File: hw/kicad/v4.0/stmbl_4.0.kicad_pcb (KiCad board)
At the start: 2 copper layers, 100 x 100 mm, 433 parts, among them J1 RJ45_LED, J2 RJ45_LED, J3 RJ45_LED, P1 USB_OTG, P10 CONN_02X06, P11 USB_OTG, P12 CONN_01X04, P13 CONN_01X04, P14 CONN_01X04, P15 CONN_01X02, P2 CONN_01X02, P3 CONN_01X02, P4 CONN_01X02, P5 CONN_01X06, P6 CONN_01X02, P7 CONN_01X04, P8 CONN_01X03, P9 CONN_01X06, Q1 IRLML6344, Q2 IRLML6344, Q3 IRLML6344, Q4 IRLML6344, Q5 IRLML6344, T1 testpoint, T2 testpoint, T44 testpoint, T45 testpoint, T46 testpoint, U1 USBLC6-4SC6, U10 SN65176B, U11 SN65176B, U12 IRAM256a, U13 ACT4088, U14 SN65176B, U15 SN65176B, U16 SN65176B, U17 SN65176B, U18 SN65176B, U19 SN65176B, U2 zldo1117, U20 USBLC6-4SC6, U21 USBLC6-4SC6, U22 USBLC6-4SC6, U23 USBLC6-4SC6, U24 non_plated, U25 STM32F303CBTx, U26 STM32F405VG, U27 ACT4088, U28 ACT4088, U29 USBLC6-4SC6, U3 SI8621, U30 non_plated, U31 non_plated, U32 non_plated, U33 heatsink, U34 fan, U35 non_plated, U36 non_plated, U37 non_plated, U39 non_plated, U4 ACT4088, U5 LNK304D, U6 LM358, U7 LM358, U8 SN65176B, U9 SN65176B, Y1 8M, Y2 8M

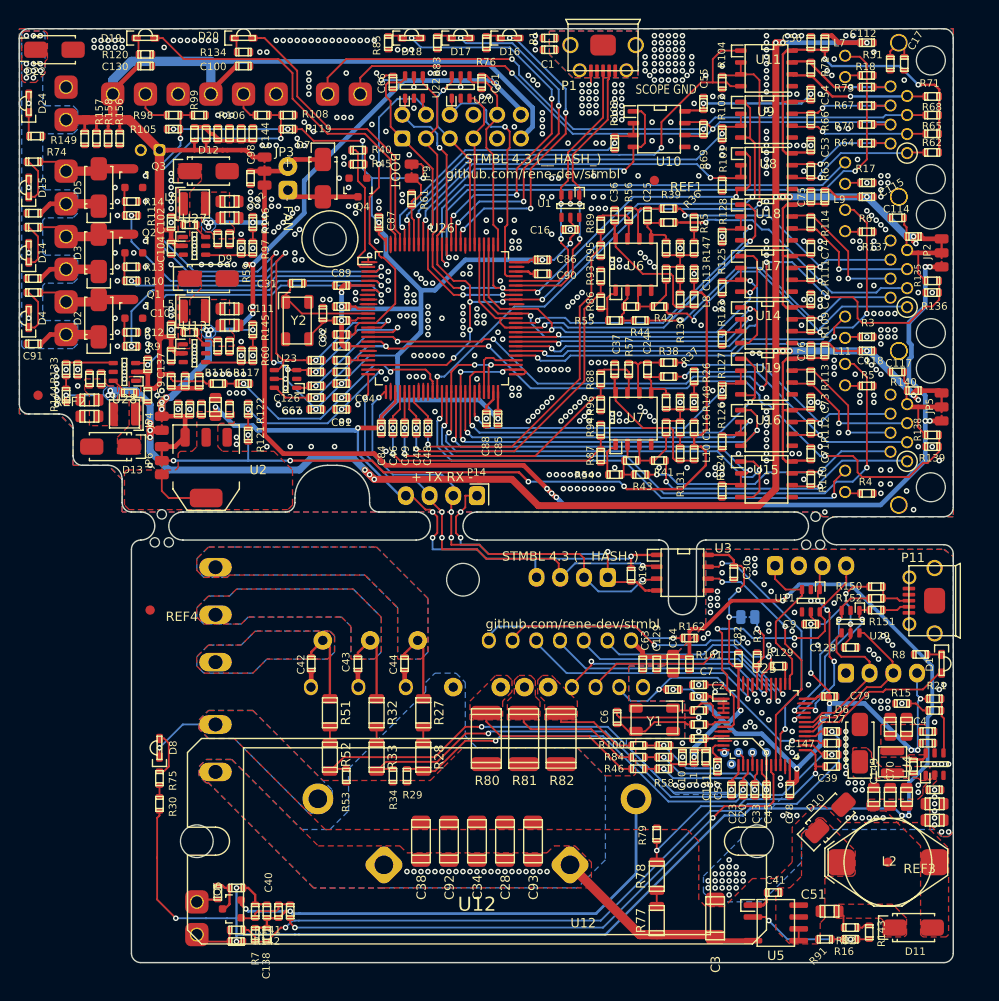
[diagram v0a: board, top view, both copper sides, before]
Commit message: Version for ST IGBT Modules
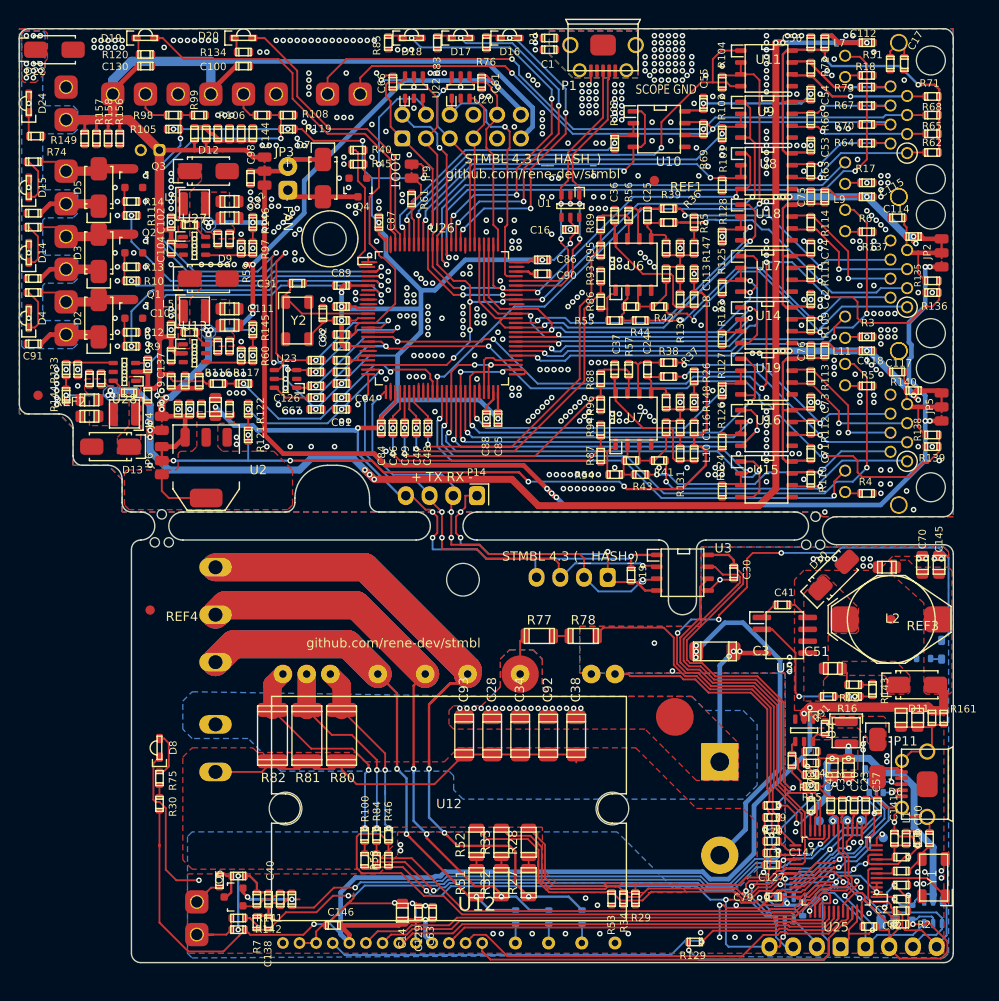
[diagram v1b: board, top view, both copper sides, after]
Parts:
- removed C22: 270µ, stmbl:C_Radial_D26_L45_P10
- removed R162: 1k, stmbl:R_0603
- added C146: 100n, stmbl:C_0603, F.Cu at (131.6, 145.8)
- C128, C9, D1, R150, R151, R152, R8, U21, U29: moved to B.Cu
- C21: value 270µ -> 560µ; footprint stmbl:C_Radial_D26_L45_P10 -> Capacitor_THT:CP_Radial_D30.0mm_P10.00mm_SnapIn
- C42, C43, C44: value 2.2µ -> 3.3µ; moved to B.Cu
- U12: value IRAM256a -> STGIBxx; footprint stmbl:IRAM256 -> stmbl:SDIP2B-26L
- moved U31 42.1 mm to (145.5, 108.8)
- moved P12 41.9 mm to (188.6, 148.0)
- moved C14 39.4 mm to (139.0, 144.4), turned to 270 degrees
- moved C129 36.9 mm to (140.8, 144.4), turned to 90 degrees
- moved JP1 35.9 mm to (191.0, 145.4)
- moved C6 35.9 mm to (195.5, 136.5)
- moved U21 35.8 mm to (195.8, 144.4), turned to 90 degrees
- moved C63 34.9 mm to (142.3, 144.4), turned to 90 degrees
- moved C42 34.9 mm to (151.1, 144.9), turned to 90 degrees
- moved Y1 34.3 mm to (195.9, 140.7), turned to 180 degrees
- moved R107 34.3 mm to (135.0, 138.8), turned to 270 degrees
- moved C43 34.0 mm to (154.7, 144.9), turned to 90 degrees
- moved C44 33.1 mm to (158.2, 144.9), turned to 90 degrees
- moved R77 33.0 mm to (153.7, 114.8), turned to 0 degrees
- moved C9 32.7 mm to (193.6, 144.4), turned to 270 degrees
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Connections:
- net /hv/f3/USB_DM renamed /hv/f3/USB_N
- net /hv/f3/USB_DP renamed /hv/f3/USB_P
- C42 pad 1: /hv/back-emf/W -> Net-(C42-Pad1)
- C42 pad 2: Net-(C42-Pad2) -> /hv/back-emf/W
- C43 pad 1: /hv/back-emf/V -> Net-(C43-Pad1)
- C43 pad 2: Net-(C43-Pad2) -> /hv/back-emf/V
- C44 pad 1: /hv/back-emf/U -> Net-(C44-Pad1)
- C44 pad 2: Net-(C44-Pad2) -> /hv/back-emf/U
- P1 pad 1: (no net) -> Net-(P1-Pad1)
- P1 pad 4: (no net) -> Net-(P1-Pad4)
- P11 pad 1: (no net) -> Net-(P11-Pad1)
- P11 pad 4: (no net) -> Net-(P11-Pad4)
- P6 pad 1: GNDPWR -> VPP
- P6 pad 2: VPP -> GNDPWR
- U1 pad 4: (no net) -> Net-(U1-Pad4)
- U1 pad 6: (no net) -> Net-(U1-Pad6)
- U12 pad 1: Net-(C42-Pad2) -> Net-(U12-Pad1)
- U12 pad 10: /hv/back-emf/U -> /hv/driver/LU
- U12 pad 13: VPP -> +15V
- U12 pad 16: /hv/driver/itirp -> GNDPWR
- U12 pad 17: /hv/driver/CUH -> Net-(U12-Pad17)
- U12 pad 18: /hv/f3/HV_EN -> /hv/driver/CWH
- U12 pad 2: /hv/back-emf/W -> Net-(C44-Pad1)
- U12 pad 20: /hv/driver/HU -> /hv/driver/CUH
- U12 pad 21: /hv/driver/CWH -> /hv/back-emf/W
- U12 pad 22: /hv/driver/HV -> /hv/back-emf/V
- U12 pad 23: /hv/driver/HW -> /hv/back-emf/U
- U12 pad 24: /hv/driver/LU -> VPP
- U12 pad 25: /hv/driver/LV -> GNDPWR
- U12 pad 26: /hv/driver/LW -> /hv/f3/A_T_HV
- U12 pad 5: Net-(C43-Pad2) -> /hv/driver/HU
- U12 pad 6: /hv/back-emf/V -> /hv/driver/HV
- U12 pad 9: Net-(C44-Pad2) -> GNDPWR
- U13 pad 3: (no net) -> Net-(U13-Pad3)
- U21 pad 4: (no net) -> Net-(U21-Pad4)
- U27 pad 3: (no net) -> Net-(U27-Pad3)
- U4 pad 3: (no net) -> Net-(U4-Pad3)
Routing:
- net GNDPWR: track 84.0 -> 325.2 mm, vias 130 -> 84
- net /hv/back-emf/U: track 8.68 -> 111.0 mm, vias 0 -> 3
- net /hv/back-emf/V: track 8.68 -> 87.0 mm, vias 0 -> 3
- net +3.3VP: track 122.8 -> 189.8 mm, vias 15 -> 16
- net /hv/back-emf/W: track 8.68 -> 73.5 mm, vias 0 -> 3
- net Net-(D1-Pad2): track 17.2 -> 79.1 mm, vias 0 -> 3
- net /hv/cur/A_IU: track 15.4 -> 73.3 mm, vias 2 -> 0
- net /hv/cur/A_IW: track 12.3 -> 66.8 mm
- net /hv/cur/A_IV: track 17.3 -> 64.2 mm, vias 2 -> 0
- net /hv/driver/LW: track 23.1 -> 54.9 mm, vias 1 -> 0
- net /hv/f3/HV_EN: track 33.3 -> 57.5 mm, vias 2 -> 1
- net /hv/driver/LV: track 25.8 -> 49.3 mm, vias 2 -> 0
- net Net-(R129-Pad2): track 1.90 -> 25.1 mm, vias 0 -> 2
- net /hv/driver/LU: track 25.6 -> 48.0 mm, vias 1 -> 0
- net /hv/driver/itirp: track 22.1 -> 0.00 mm, vias 1 -> 0
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- removed copper zone on B.Cu, net /hv/back-emf/U
- removed copper zone on F.Cu, net /hv/back-emf/U
- removed copper zone on B.Cu, net /hv/back-emf/V
- removed copper zone on F.Cu, net /hv/back-emf/V
- removed copper zone on B.Cu, net /hv/back-emf/W
- removed copper zone on F.Cu, net /hv/back-emf/W
- removed copper zone on F.Cu, net /hv/driver/CUH
- removed copper zone on F.Cu, net /hv/driver/CVH
- removed copper zone on F.Cu, net /hv/driver/CWH
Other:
- board text added: "+"
- board text added: "BW BV BU HU HV HW + G LU LV LW + EN GND"
- board text added: "RST DIO CK"
- board text added: "TH GND VPP U V W CWH CVH CUH"
- board text removed: "+ +"
- board text removed: "-"
- board text removed: "- -"
- board text removed: "- TH LV HW W- V- U- + UB VB WB"
- board text removed: "15V LW LU HV HU EN iT U V W"
- board text removed: "C22"
- board text removed: "RST DIO - CK"
- board text removed: "V U D W"

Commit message: changed orientation of IGBT module, other improvements
* removed USB port
* better power distribution for F3
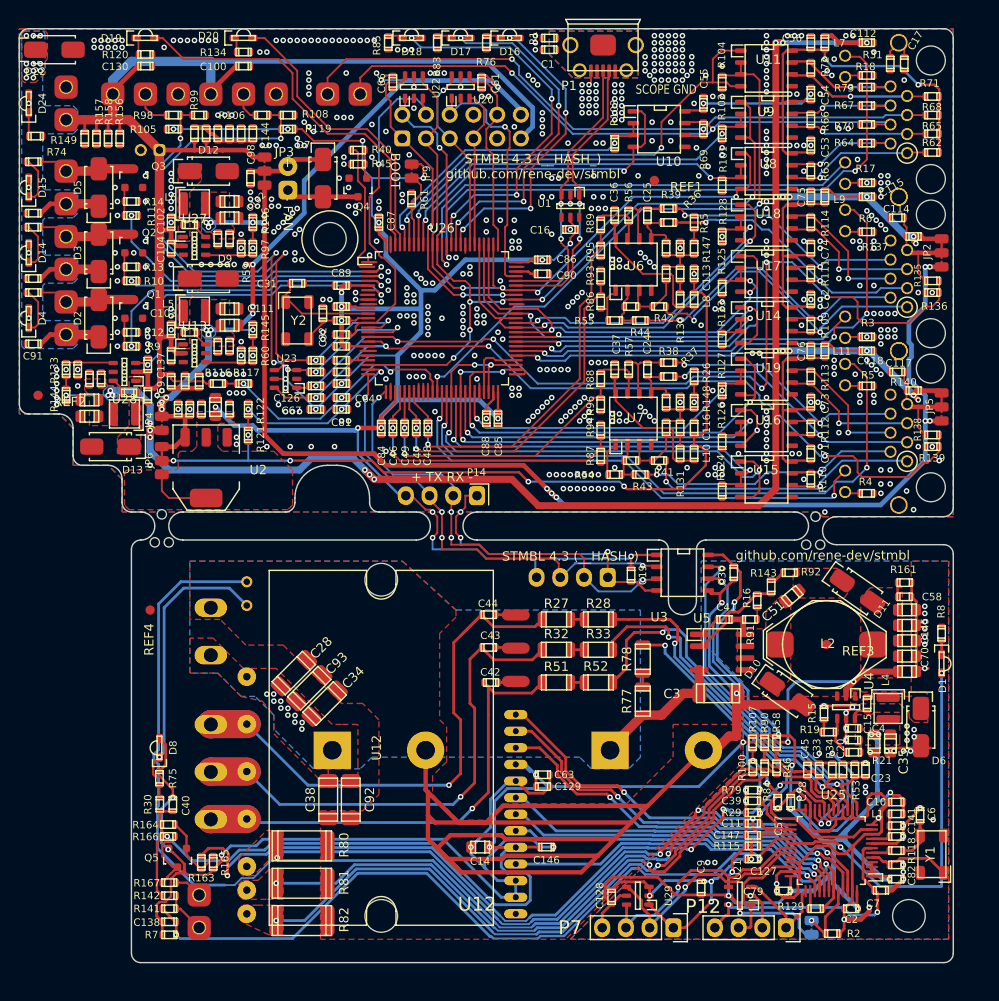
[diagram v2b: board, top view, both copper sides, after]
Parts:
- removed P11: USB_OTG, stmbl:USB_Micro-B
- removed R150: 1.5k, stmbl:R_0603
- removed R151, R152: 22, stmbl:R_0603
- removed T1, T2, T44, T45, T46: testpoint, stmbl:Measurement_Point_Round-SMD-Pad_Small
- added C22: 270µ, Capacitor_THT:CP_Radial_D26.0mm_P10.00mm_SnapIn, B.Cu at (131.5, 127.0)
- C128, C42, C43, C44, C9, D1, P12, P7, R8, U21, U29: moved to F.Cu
- C21: value 560µ -> 270µ; footprint Capacitor_THT:CP_Radial_D30.0mm_P10.00mm_SnapIn -> Capacitor_THT:CP_Radial_D26.0mm_P10.00mm_SnapIn
- moved U31 59.8 mm to (193.2, 144.8)
- moved R58 43.4 mm to (179.1, 126.2), turned to 90 degrees
- moved R90 43.4 mm to (177.8, 126.2), turned to 90 degrees
- moved R107 43.4 mm to (176.5, 126.2), turned to 90 degrees
- moved R100 42.2 mm to (176.5, 128.9), turned to 270 degrees
- moved R46 42.2 mm to (179.1, 128.9), turned to 270 degrees
- moved R84 42.2 mm to (177.8, 128.9), turned to 270 degrees
- moved U30 34.8 mm to (136.8, 108.8)
- moved C44 33.9 mm to (148.2, 112.5), turned to 180 degrees
- moved C43 29.6 mm to (148.2, 116.0), turned to 180 degrees
- moved R53 29.5 mm to (187.5, 129.1), turned to 90 degrees
- moved R27 28.3 mm to (155.5, 113.0), turned to 0 degrees
- moved C38 27.4 mm to (131.1, 132.3)
- moved R34 26.3 mm to (185.0, 129.1), turned to 90 degrees
- moved R32 25.6 mm to (155.5, 116.2), turned to 0 degrees
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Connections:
- P6 pad 1: VPP -> GNDPWR
- P6 pad 2: GNDPWR -> VPP
- U25 pad 12: Net-(T44-Pad1) -> GNDPWR
- U25 pad 14: Net-(T45-Pad1) -> GNDPWR
- U25 pad 16: Net-(T46-Pad1) -> GNDPWR
- U25 pad 19: Net-(T1-Pad1) -> GNDPWR
- U25 pad 32: /hv/f3/USB_N -> GNDPWR
- U25 pad 33: /hv/f3/USB_P -> GNDPWR
- U29 pad 1: /hv/f3/USB_N -> GNDPWR
- U29 pad 3: /hv/f3/USB_P -> GNDPWR
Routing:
- net GNDPWR: track 325.2 -> 470.2 mm, vias 84 -> 60
- net /hv/f3/A_T_HV: track 35.9 -> 120.1 mm, vias 2 -> 3
- net /hv/cur/A_IU: track 73.3 -> 11.8 mm
- net /hv/cur/A_IV: track 64.2 -> 11.7 mm
- net /hv/back-emf/U: track 111.0 -> 63.9 mm, vias 3 -> 1
- net /hv/cur/A_IW: track 66.8 -> 21.0 mm
- net /hv/driver/CUH: track 19.4 -> 65.0 mm
- net /hv/driver/CVH: track 20.9 -> 64.9 mm
- net /hv/driver/CWH: track 24.0 -> 64.6 mm
- net Net-(D1-Pad2): track 79.1 -> 41.4 mm, vias 3 -> 2
- net +3.3VP: track 189.8 -> 152.3 mm, vias 16 -> 13
- net /hv/back-emf/V: track 87.0 -> 57.3 mm, vias 3 -> 1
- net /hv/f3/USB_N: track 24.9 -> 0.00 mm, vias 1 -> 0
- net /hv/f3/USB_P: track 24.8 -> 0.00 mm, vias 1 -> 0
- net Net-(R129-Pad2): track 25.1 -> 1.96 mm, vias 2 -> 0
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- added copper zone on F.Cu, net /hv/driver/CUH
- added copper zone on F.Cu, net /hv/driver/CVH
- added copper zone on F.Cu, net /hv/driver/CWH
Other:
- net class Default: trace_width 0.2 -> 0.3
- net class UVW: trace_width 0.25 -> 0.3
- net class UVW_L: trace_width 0.25 -> 0.3
- board text added: "+ +"
- board text added: "-"
- board text added: "C22"
- board text added: "HOT GROUND!"
- board text added: "RST DIO - CK"
- board text added: "V U D W"
- board text removed: "+"
- board text removed: "BW BV BU HU HV HW + G LU LV LW + EN GND"
- board text removed: "HOT GROUND!!!"
- board text removed: "P2"
- board text removed: "P6"
- board text removed: "P8"
- board text removed: "RST DIO CK"
- board text removed: "TH GND VPP U V W CWH CVH CUH"

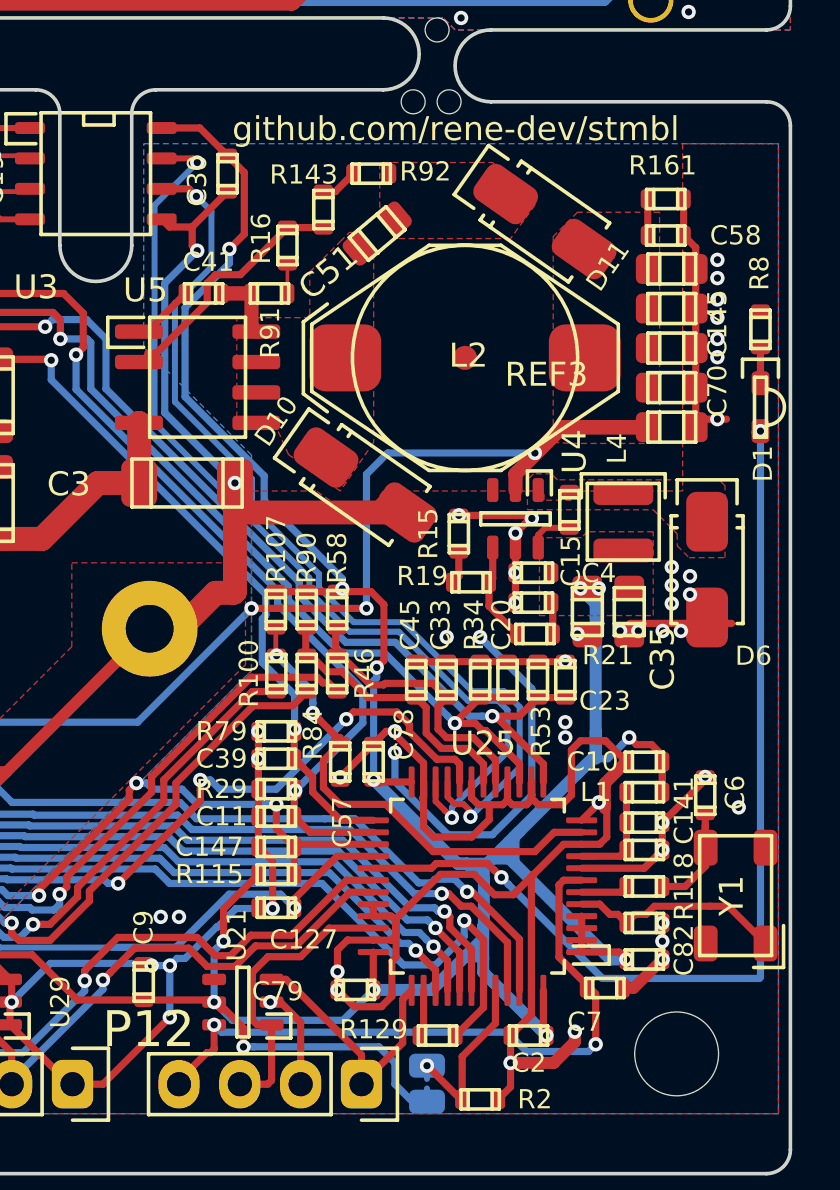
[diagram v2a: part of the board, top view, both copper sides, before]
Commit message: improved ground plane
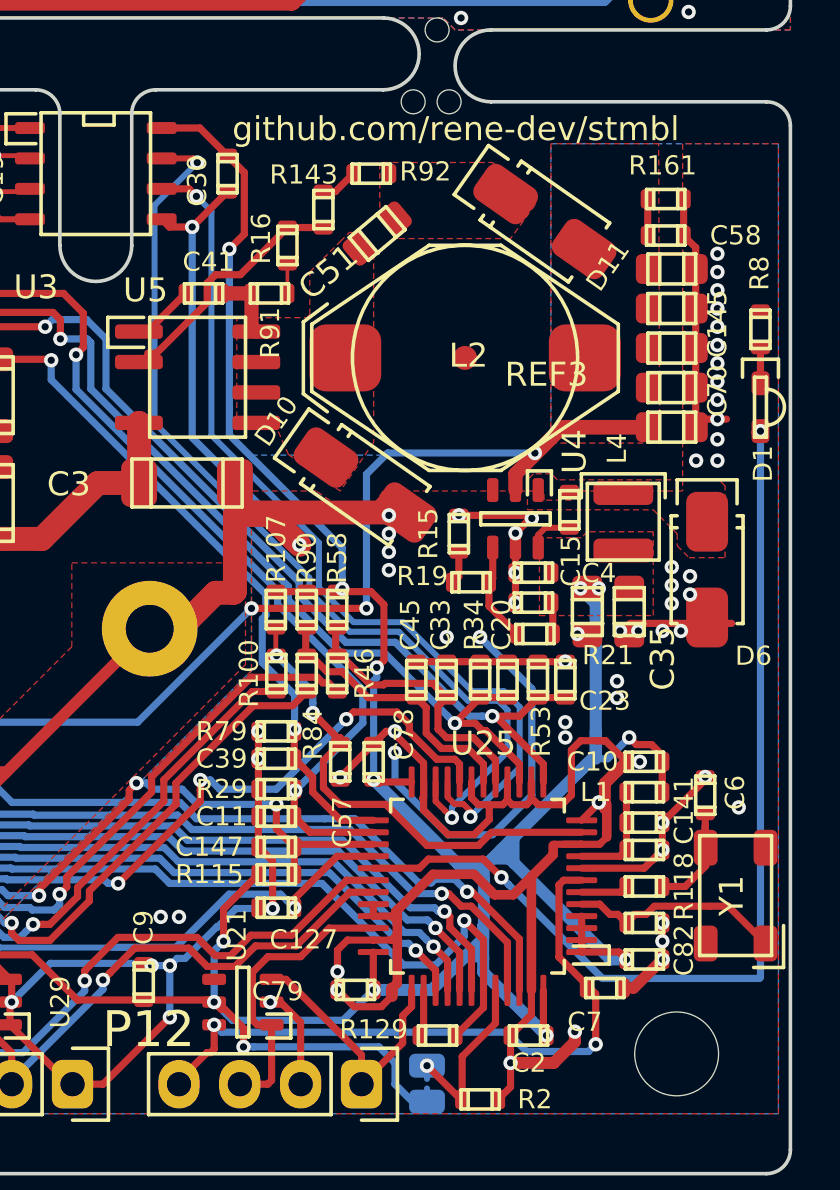
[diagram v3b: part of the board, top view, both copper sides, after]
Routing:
- net GNDPWR: track 470.2 -> 475.9 mm, vias 60 -> 73
- net +3.3VP: track 152.3 -> 150.8 mm
- net /hv/f3/HV_TX: track 39.2 -> 38.0 mm
